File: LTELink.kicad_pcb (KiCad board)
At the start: 4 copper layers, 93.3 x 65.8 mm, 95 parts, among them IC1 RTL8305NB-VC-CG, J1 DF40HC(3.0)-100DS-0.4V(51), J2 DF40HC(3.0)-100DS-0.4V(51), J3 DF40HC(3.0)-100DS-0.4V(51), J4 1759547-1, J5 USB_A, J6 Conn_01x03_Pin, J7 Micro_SD_Card_Det1, J8 USB_A, J9 USB_C_Receptacle_USB2.0_16P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

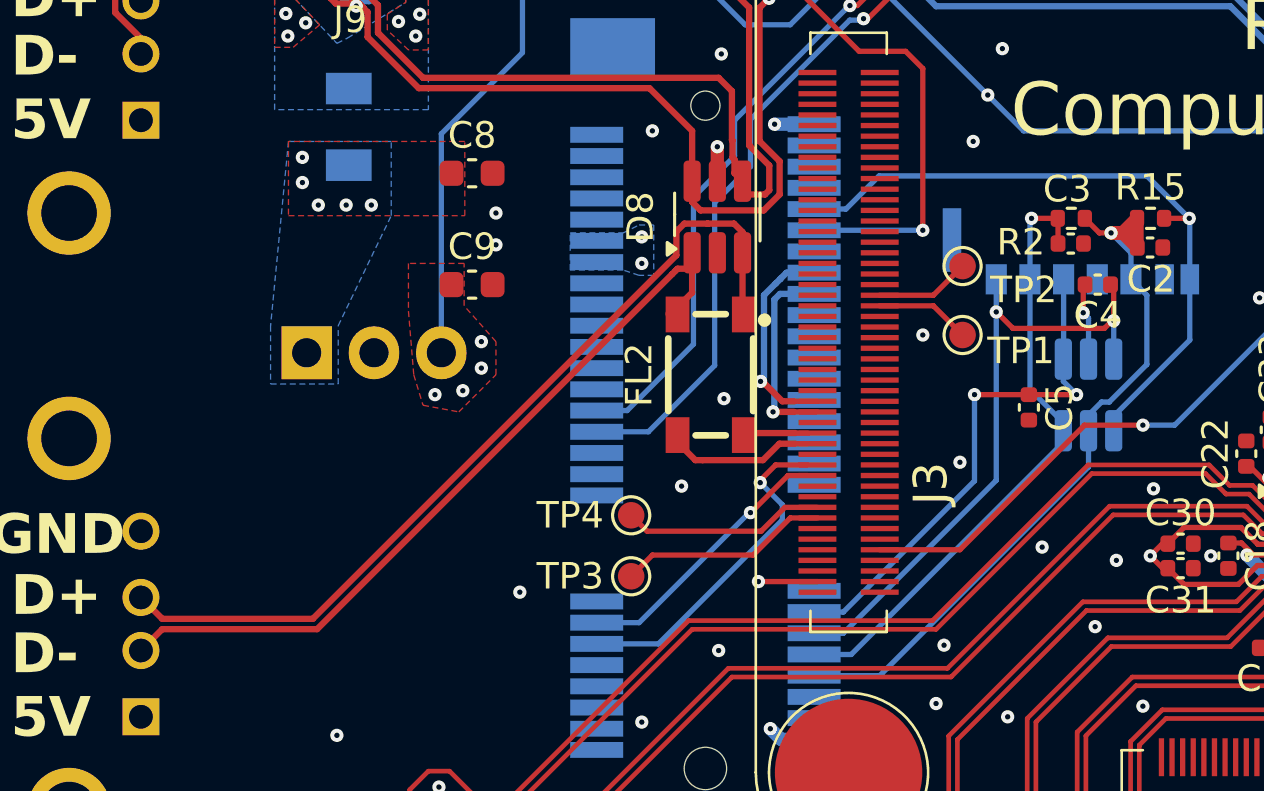
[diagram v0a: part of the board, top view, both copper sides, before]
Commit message: Finalized layout, added more detailed 3d models
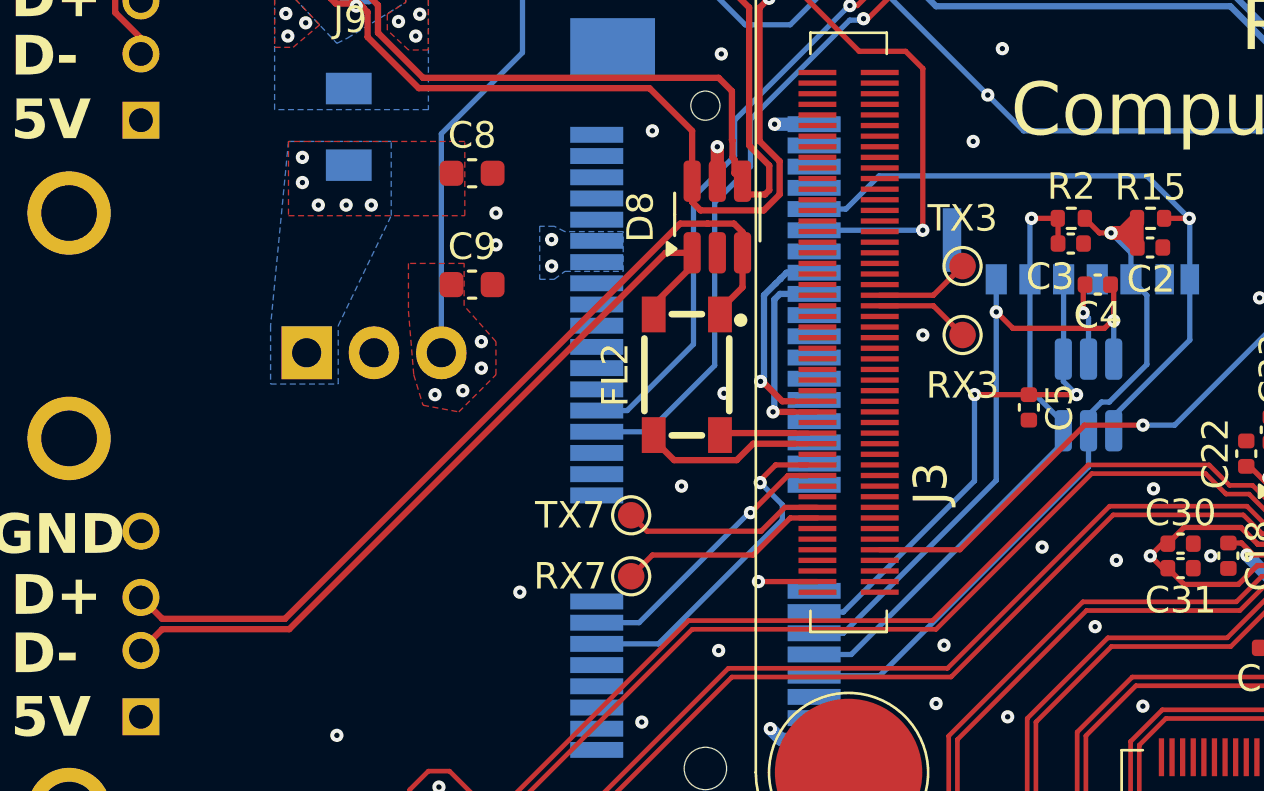
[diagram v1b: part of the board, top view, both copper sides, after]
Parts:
- J1, J2, J3: value DF40HC(3.0)-100DS-0.4V(51) -> DF40C100DS04V51
- moved FL2 0.90 mm to (182.3, 79.6)
- renumbered TP1 to RX3, TP3 to RX7, TP2 to TX3, TP4 to TX7
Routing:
- net /USB/J8_D-: track 28.3 -> 29.9 mm
- net /Compute Module/USB2_HOST3_D-: track 5.37 -> 6.56 mm
- net /Compute Module/USB2_HOST3_D+: track 2.44 -> 3.34 mm
- net GND: vias 72 -> 71
